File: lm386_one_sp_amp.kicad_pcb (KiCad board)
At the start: 2 copper layers, 44 x 45.3 mm, 14 parts, among them U1 LM386

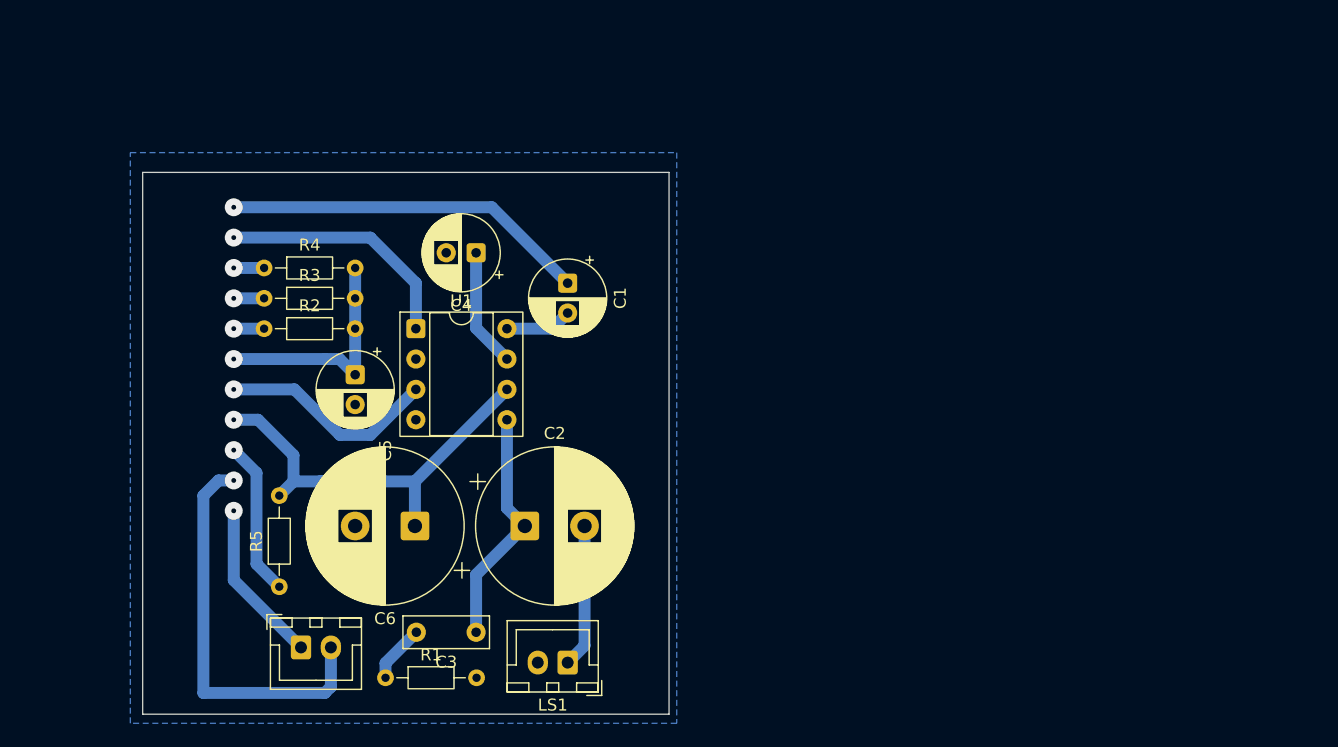
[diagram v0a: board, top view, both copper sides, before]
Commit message: ギター接続向けに回路を変更
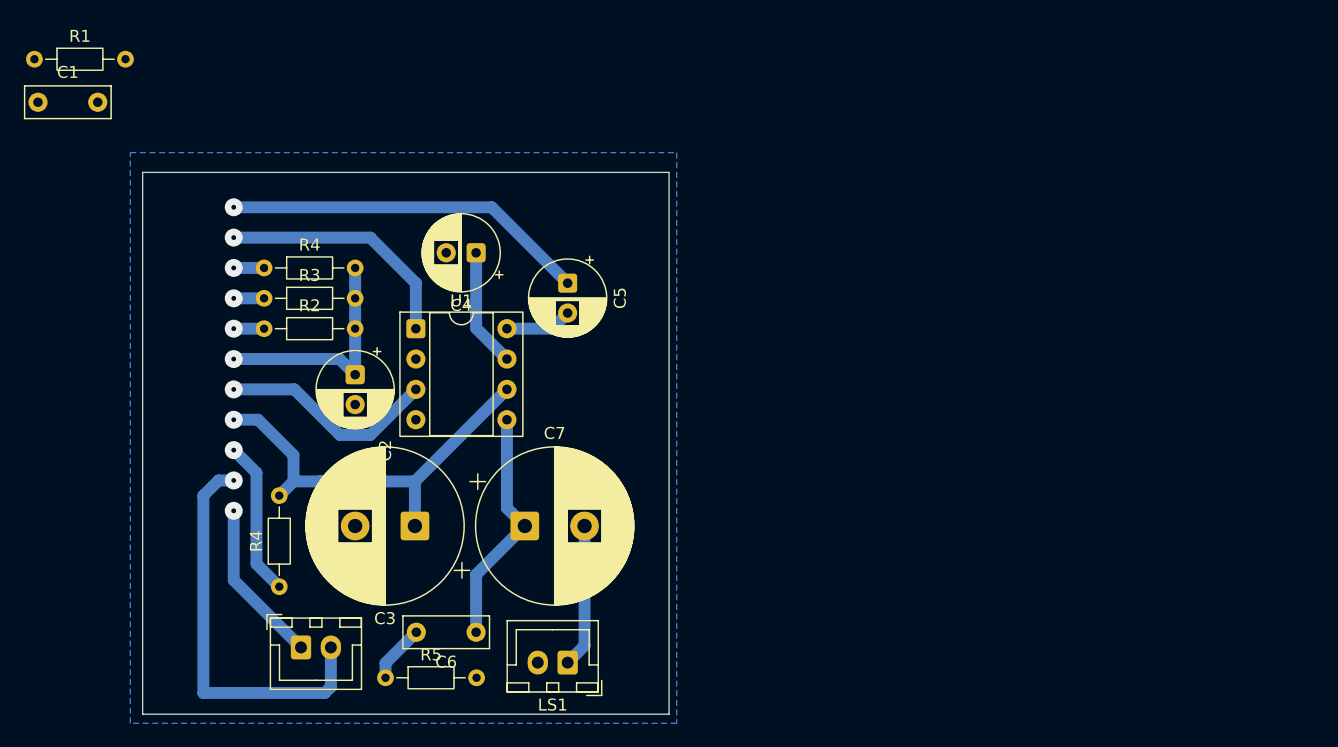
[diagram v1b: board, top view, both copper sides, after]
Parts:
- added C1: 0.1uF, Capacitor_THT:C_Disc_D7.0mm_W2.5mm_P5.00mm, F.Cu at (87.8, 62.3)
- added R1: 1M, Resistor_THT:R_Axial_DIN0204_L3.6mm_D1.6mm_P7.62mm_Horizontal, F.Cu at (87.5, 58.7)
- renumbered C5 to C2, C6 to C3, C1 to C5, C3 to C6, C2 to C7, R5 to R4, R1 to R5
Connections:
- C2 pad 1: Net-(C5-Pad1) -> Net-(C2-Pad1)
- C5 pad 1: Net-(C1-Pad1) -> Net-(C5-Pad1)
- R2 pad 2: Net-(C5-Pad1) -> Net-(C2-Pad1)
- R3 pad 2: Net-(C5-Pad1) -> Net-(C2-Pad1)
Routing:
- net Net-(C5-Pad1): track 19.5 -> 49.9 mm, vias 1 -> 2
- net Net-(C1-Pad1): track 30.4 -> 0.00 mm, vias 1 -> 0

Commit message: 基板を作り直す
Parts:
- removed the R4 at (106.7, 76.2)
- removed the R4 at (108.0, 102.9)
- added R4: 4.7k, Resistor_THT:R_Axial_DIN0204_L3.6mm_D1.6mm_P7.62mm_Horizontal, F.Cu at (154.3, 83.8)
- added R6: 1.5k, Resistor_THT:R_Axial_DIN0204_L3.6mm_D1.6mm_P7.62mm_Horizontal, F.Cu at (180.3, 86.4)
- added R7: 10, Resistor_THT:R_Axial_DIN0204_L3.6mm_D1.6mm_P7.62mm_Horizontal, F.Cu at (164.5, 91.4)
- C1: footprint Capacitor_THT:C_Disc_D7.0mm_W2.5mm_P5.00mm -> Capacitor_THT:C_Rect_L10.3mm_W5.0mm_P7.50mm_MKS4
- C6: footprint Capacitor_THT:C_Disc_D7.0mm_W2.5mm_P5.00mm -> Capacitor_THT:C_Rect_L9.0mm_W4.0mm_P7.50mm_MKT
- R1: value 1M -> 4.7k
- R3: value 4.7k -> 1M
- R5: value 10 -> 4.7k
- moved C1 98.8 mm to (185.5, 76.8)
- moved BT1 80.8 mm to (188.0, 87.6), turned to 90 degrees
- moved R3 71.4 mm to (177.8, 72.4)
- moved R1 69.1 mm to (154.3, 76.2)
- moved C3 63.6 mm to (182.9, 99.3), turned to -90 degrees
- moved C2 53.1 mm to (166.4, 74.9), turned to 90 degrees
- moved C6 51.2 mm to (174.6, 96.5)
- moved C4 50.2 mm to (174.6, 73.7)
- moved C5 49.7 mm to (181.6, 81.3), turned to 180 degrees
- moved U1 48.3 mm to (167.6, 81.3)
- moved R2 47.7 mm to (154.3, 78.7)
- moved R5 44.6 mm to (154.3, 86.4)
- moved C7 35.9 mm to (163.8, 104.1), turned to 180 degrees
- moved LS1 30.2 mm to (158.1, 93.9), turned to 90 degrees
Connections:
- R1 pad 1: GND -> Net-(J1-PadT)
- R1 pad 2: Net-(C1-Pad2) -> Net-(C2-Pad1)
- R3 pad 1: Net-(J1-PadR) (its old number) -> GND
- R3 pad 2: Net-(C2-Pad1) -> Net-(C1-Pad2)
- R5 pad 1: Net-(C6-Pad2) -> Net-(U1-+)
- R5 pad 2: GND -> Net-(R5-Pad2)
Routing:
- net Net-(C5-Pad1): track 49.9 -> 0.00 mm, vias 2 -> 0
- net Net-(SW1-B): track 35.3 -> 0.00 mm, vias 1 -> 0
- net GND: track 33.8 -> 0.00 mm, vias 1 -> 0
- net Net-(U1-GAIN-Pad1): track 20.6 -> 0.00 mm, vias 1 -> 0
- net Net-(C6-Pad1): track 20.1 -> 0.00 mm
- net Net-(U1-+): track 18.2 -> 0.00 mm, vias 1 -> 0
- net Net-(BT1-+): track 13.8 -> 0.00 mm, vias 1 -> 0
- net Net-(D1-A): track 13.0 -> 0.00 mm, vias 1 -> 0
- net Net-(C7-Pad2): track 12.0 -> 0.00 mm
- net Net-(U1-BYPASS): track 9.96 -> 0.00 mm
- net Net-(C5-Pad2): track 5.62 -> 0.00 mm
- net Net-(C6-Pad2): track 4.88 -> 0.00 mm
- net Net-(J2-PadT): track 2.54 -> 0.00 mm, vias 1 -> 0
- net Net-(J1-PadR) (its old number): track 2.54 -> 0.00 mm, vias 1 -> 0
- net Net-(J1-PadR): track 2.54 -> 0.00 mm, vias 1 -> 0
- removed copper zone on B.Cu, net GND
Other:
- board outline removed
